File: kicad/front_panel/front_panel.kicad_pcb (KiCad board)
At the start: 2 copper layers, 0 parts

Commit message: fix dru
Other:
- board outline added: 203.2 x 66 mm
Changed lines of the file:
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@@
 	(title_block
 		(title "SW32 - Front Panel")
-		(date "2024-05-27")
+		(date "2024-05-31")
 		(rev "1")
 		(company "saawsm")
@@
 	)
 	(net 0 "")
+	(gr_rect
+		(start 48.26 60.96)
+		(end 251.46 127)
+		(stroke
+			(width 0.05)
+			(type default)
+		)
+		(fill none)
+		(layer "Edge.Cuts")
+	)
 )

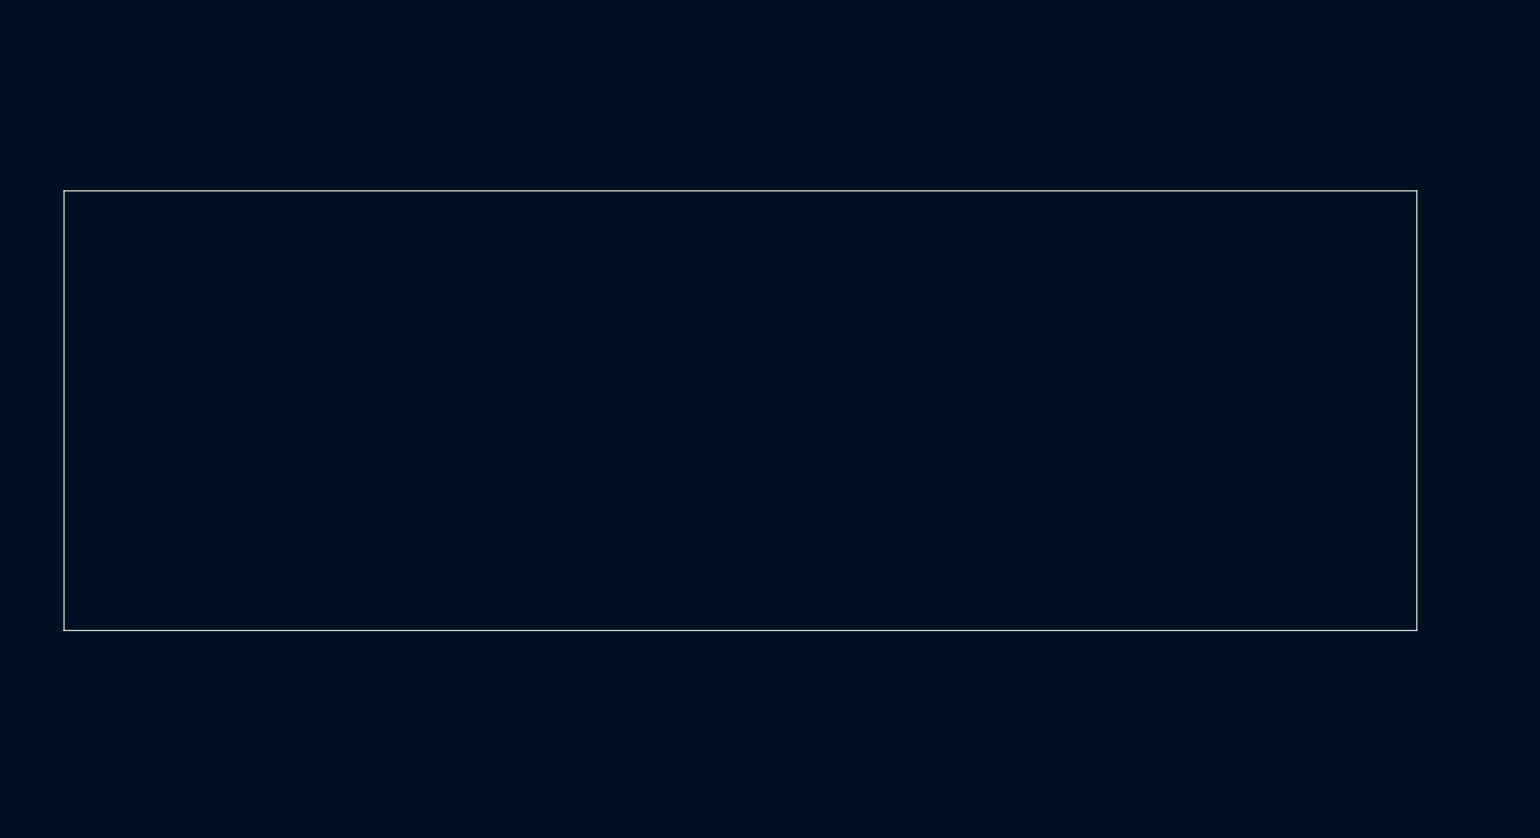
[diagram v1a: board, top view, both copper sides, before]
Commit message: add front panel
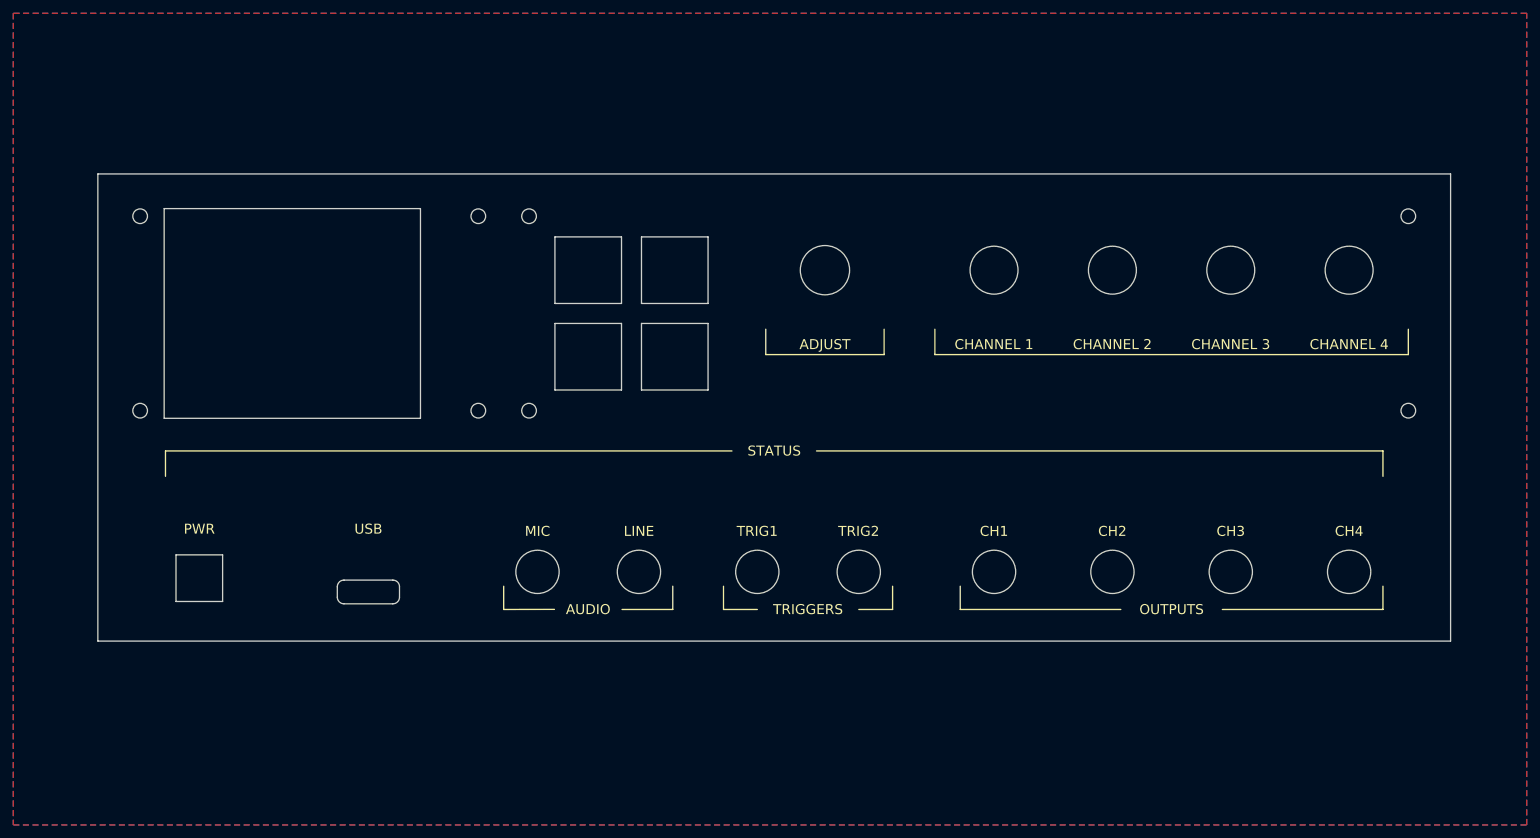
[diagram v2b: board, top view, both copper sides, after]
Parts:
- added H1: MountingHole, MountingHole:MountingHole_2.2mm_M2, F.Cu at (59.7, 64.8)
- added H2: MountingHole, MountingHole:MountingHole_2.2mm_M2, F.Cu at (118.1, 64.8)
- added H3: MountingHole, MountingHole:MountingHole_2.2mm_M2, F.Cu at (110.5, 94.0)
- added H4: MountingHole, MountingHole:MountingHole_2.2mm_M2, F.Cu at (250.2, 64.8)
- added H5: MountingHole, MountingHole:MountingHole_2.2mm_M2, F.Cu at (59.7, 94.0)
- added H6: MountingHole, MountingHole:MountingHole_2.2mm_M2, F.Cu at (118.1, 94.0)
- added H7: MountingHole, MountingHole:MountingHole_2.2mm_M2, F.Cu at (110.5, 64.8)
- added H8: MountingHole, MountingHole:MountingHole_2.2mm_M2, F.Cu at (250.2, 94.0)
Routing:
- added copper zone on B.Cu, net (none)
- added copper zone on F.Cu, net (none)
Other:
- board size 203.2 x 66 mm -> 203.2 x 70.2 mm
- board text added: "ADJUST"
- board text added: "AUDIO"
- board text added: "CH1"
- board text added: "CH2"
- board text added: "CH3"
- board text added: "CH4"
- board text added: "CHANNEL 1"
- board text added: "CHANNEL 2"
- board text added: "CHANNEL 3"
- board text added: "CHANNEL 4"
- board text added: "JLCJLCJLCJLC"
- board text added: "LINE"
- board text added: "MIC"
- board text added: "OUTPUTS"
- board text added: "PWR"
- board text added: "STATUS"
- board text added: "SW32 ${PROJECTNAME} rev${REVISION} ${hash}"
- board text added: "TRIG1"
- board text added: "TRIG2"
- board text added: "TRIGGERS"
- board text added: "USB"

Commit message: add box name
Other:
- board text added: "SW32"
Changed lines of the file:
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@@
 	(title_block
 		(title "SW32 - Front Panel")
-		(date "2024-06-11")
+		(date "2024-06-12")
 		(rev "1")
 		(company "saawsm")
@@
 	)
 	(gr_line
+		(start 87.63 97.536)
+		(end 90.805 97.536)
+		(stroke
+			(width 0.2)
+			(type solid)
+		)
+		(layer "F.SilkS")
+	)
+	(gr_line
 		(start 250.19 81.745)
 		(end 250.19 85.555)
@@
 		(end 246.379999 123.84175)
 		(locked yes)
+		(stroke
+			(width 0.2)
+			(type solid)
+		)
+		(layer "F.SilkS")
+	)
+	(gr_line
+		(start 74.295 97.536)
+		(end 77.47 97.536)
 		(stroke
 			(width 0.2)
@@
 		)
 	)
+	(gr_text "SW32"
+		(at 82.55 98.425 0)
+		(layer "F.SilkS")
+		(effects
+			(font
+				(size 1.5 1.5)
+				(thickness 0.3)
+				(bold yes)
+			)
+			(justify bottom)
+		)
+	)

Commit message: fix title block
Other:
- board text added: "${TITLE} ${PROJECTNAME} rev${REVISION} ${hash}"
- board text removed: "SW32 ${PROJECTNAME} rev${REVISION} ${hash}"
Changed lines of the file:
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@@
 	(paper "A4")
 	(title_block
-		(title "SW32 - Front Panel")
+		(title "SW32")
 		(date "2024-06-12")
 		(rev "1")
@@
 		(start 87.63 97.536)
 		(end 90.805 97.536)
+		(locked yes)
 		(stroke
 			(width 0.2)
@@
 		(start 74.295 97.536)
 		(end 77.47 97.536)
+		(locked yes)
 		(stroke
 			(width 0.2)
@@
 		(layer "Edge.Cuts")
 	)
-	(gr_text "SW32\n${PROJECTNAME}\nrev${REVISION} ${hash}"
+	(gr_text "${TITLE}\n${PROJECTNAME}\nrev${REVISION} ${hash}"
 		(locked yes)
 		(at 180.34 82.55 0)
@@
 	)
 	(gr_text "SW32"
+		(locked yes)
 		(at 82.55 98.425 0)
 		(layer "F.SilkS")
@@
 	(dimension
 		(type orthogonal)
+		(locked yes)
 		(layer "Dwgs.User")
 		(pts
@@
 		(orientation 1)
 		(gr_text "70.1709 mm"
+			(locked yes)
 			(at 261.94 93.505473 90)
 			(layer "Dwgs.User")
@@
 	(dimension
 		(type orthogonal)
+		(locked yes)
 		(layer "Dwgs.User")
 		(pts
@@
 		(orientation 0)
 		(gr_text "203.2000 mm"
+			(locked yes)
 			(at 154.94 52.39 0)
 			(layer "Dwgs.User")
